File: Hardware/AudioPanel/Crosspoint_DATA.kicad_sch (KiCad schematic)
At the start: 18 parts, among them SW4 ~{RESET}, U18 MT8816AP1, U28 MCP23017_ML, U34 ICL7660, U47 MT8816AP1

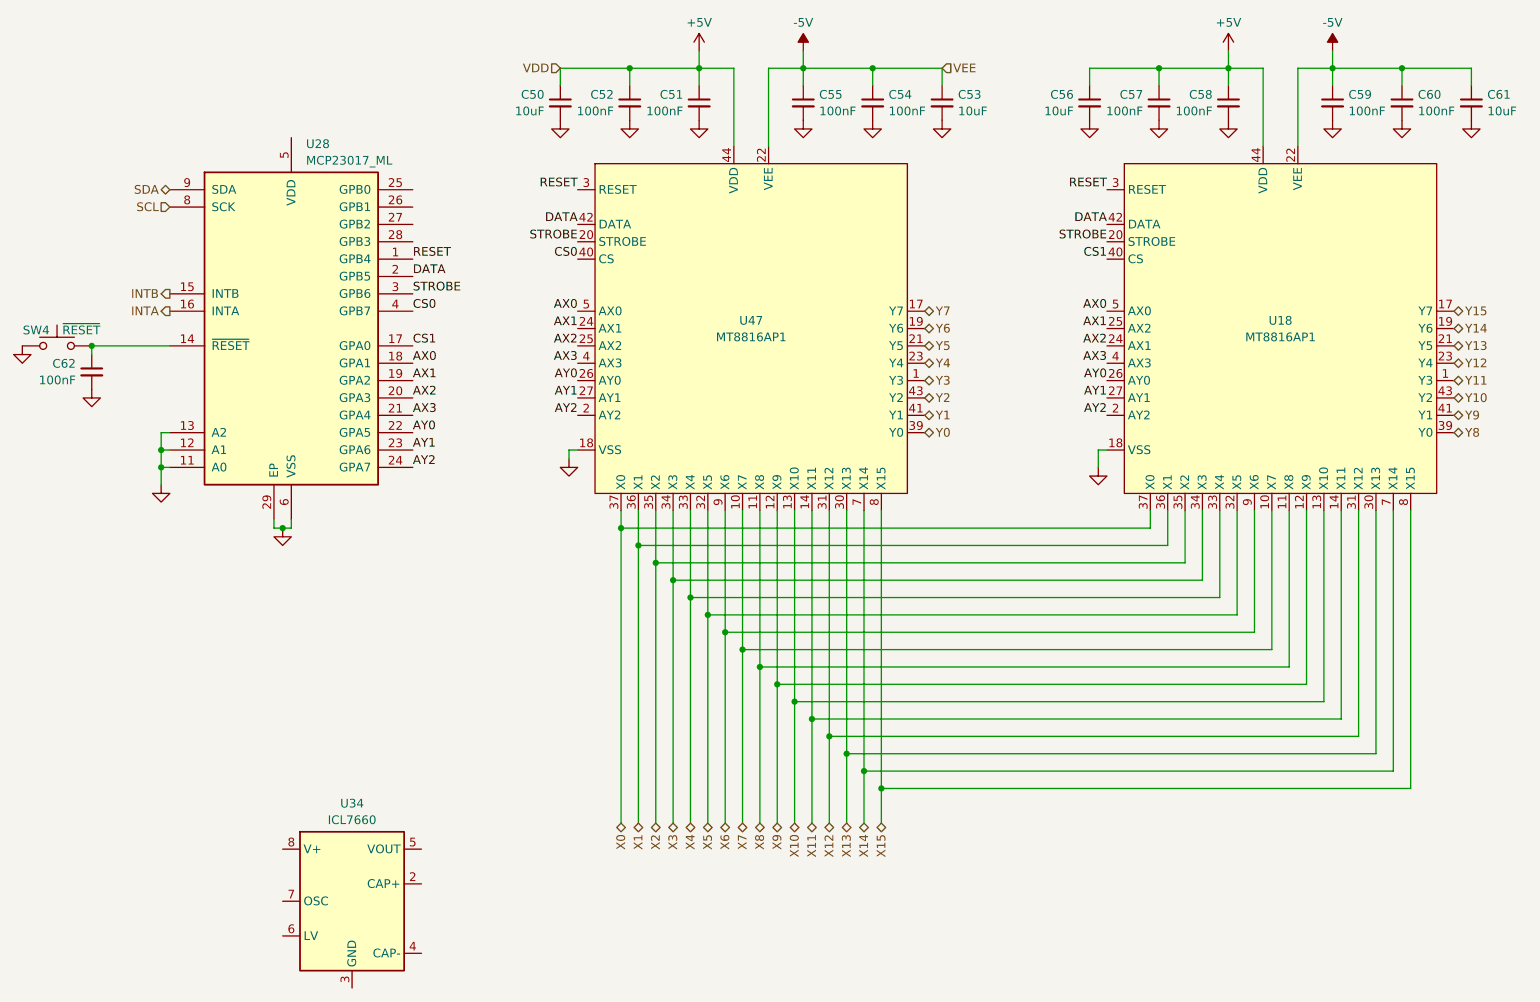
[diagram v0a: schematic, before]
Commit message: Added crosspoints for each connector
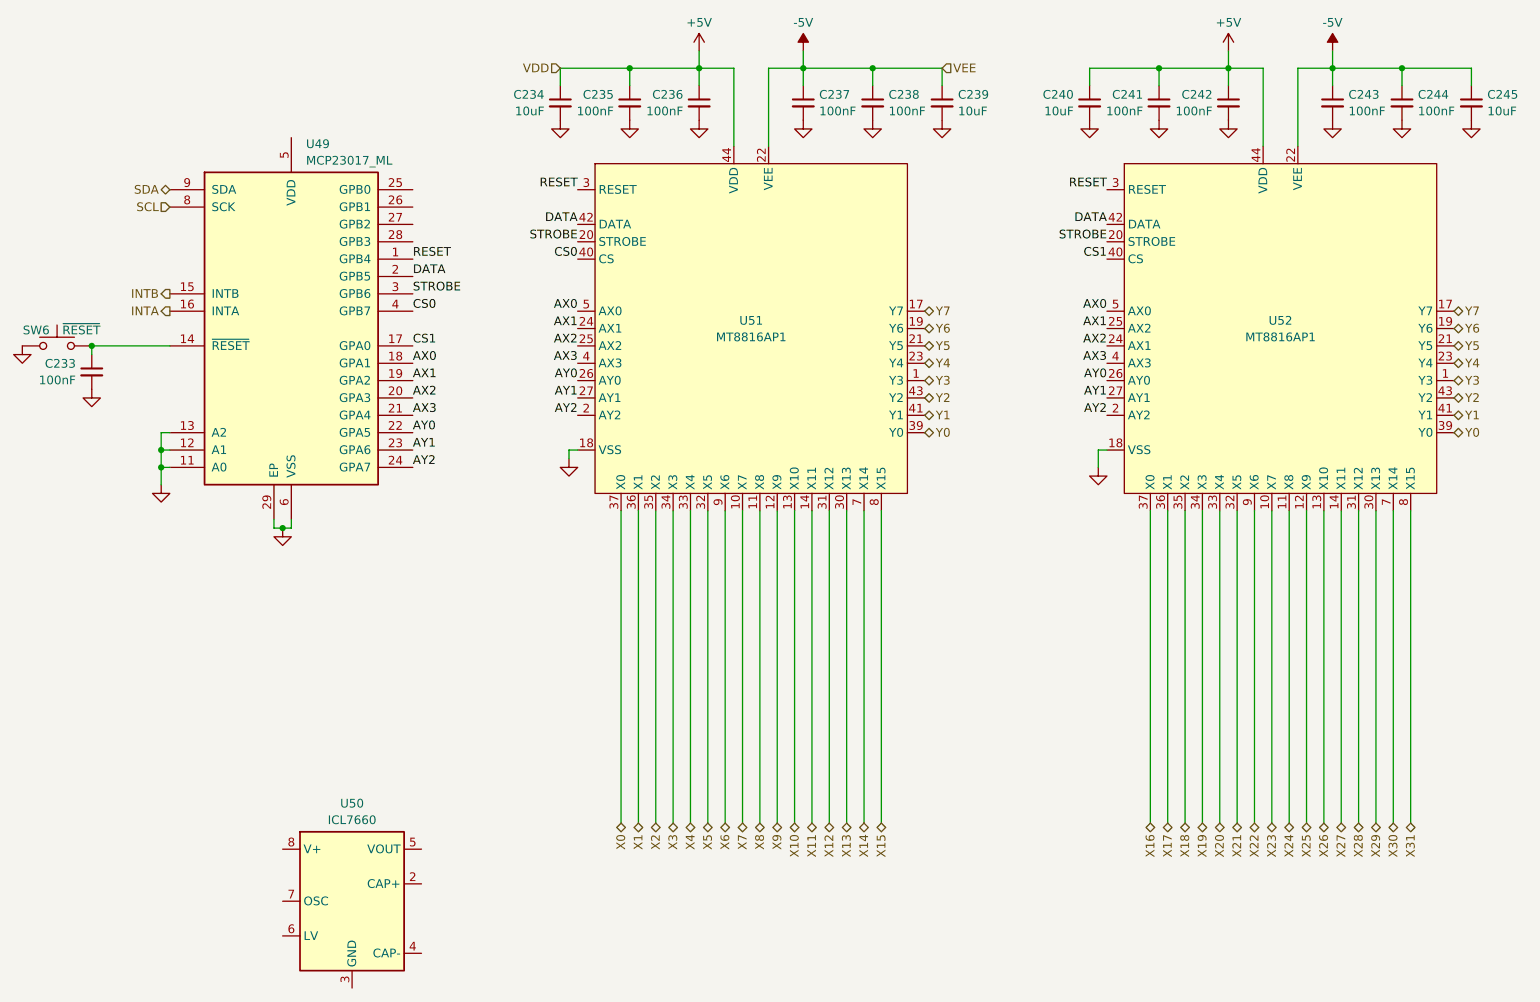
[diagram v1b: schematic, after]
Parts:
- renumbered C62 to C233, C50 to C234, C52 to C235, C51 to C236, C55 to C237, C54 to C238, C53 to C239, C56 to C240, C57 to C241, C58 to C242, C59 to C243, C60 to C244, C61 to C245, SW4 to SW6, U28 to U49, U34 to U50, U47 to U51, U18 to U52
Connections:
- net Y10 is gone; now on net Y2: U52.43 (Y2)
- net Y11 is gone; now on net Y3: U52.1 (Y3)
- net Y12 is gone; now on net Y4: U52.23 (Y4)
- net Y13 is gone; now on net Y5: U52.21 (Y5)
- net Y14 is gone; now on net Y6: U52.19 (Y6)
- net Y15 is gone; now on net Y7: U52.17 (Y7)
- net Y8 is gone; now on net Y0: U52.39 (Y0)
- net Y9 is gone; now on net Y1: U52.41 (Y1)
- net X0: no longer U52.37 (X0)
- net X1: no longer U52.36 (X1)
- net X10: no longer U52.13 (X10)
- net X11: no longer U52.14 (X11)
- net X12: no longer U52.31 (X12)
- net X13: no longer U52.30 (X13)
- net X14: no longer U52.7 (X14)
- net X15: no longer U52.8 (X15)
- net X2: no longer U52.35 (X2)
- net X3: no longer U52.34 (X3)
- net X4: no longer U52.33 (X4)
- net X5: no longer U52.32 (X5)
- net X6: no longer U52.9 (X6)
- net X7: no longer U52.10 (X7)
- net X8: no longer U52.11 (X8)
- net X9: no longer U52.12 (X9)
- new net X16: U52.37 (X0)
- new net X17: U52.36 (X1)
- new net X18: U52.35 (X2)
- new net X19: U52.34 (X3)
- new net X20: U52.33 (X4)
- new net X21: U52.32 (X5)
- new net X22: U52.9 (X6)
- new net X23: U52.10 (X7)
- new net X24: U52.11 (X8)
- new net X25: U52.12 (X9)
- new net X26: U52.13 (X10)
- new net X27: U52.14 (X11)
- new net X28: U52.31 (X12)
- new net X29: U52.30 (X13)
- new net X30: U52.7 (X14)
- new net X31: U52.8 (X15)
